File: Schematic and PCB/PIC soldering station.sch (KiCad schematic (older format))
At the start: 69 parts, among them J1 DC_INLET, K2 hakko 907, P1 24VAC, Q1 2N3904, Q2 2N3906, Q3 IRLR2908, SW2 BUTTON1, SW3 BUTTON2, U1 LM358, U2 LM7812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

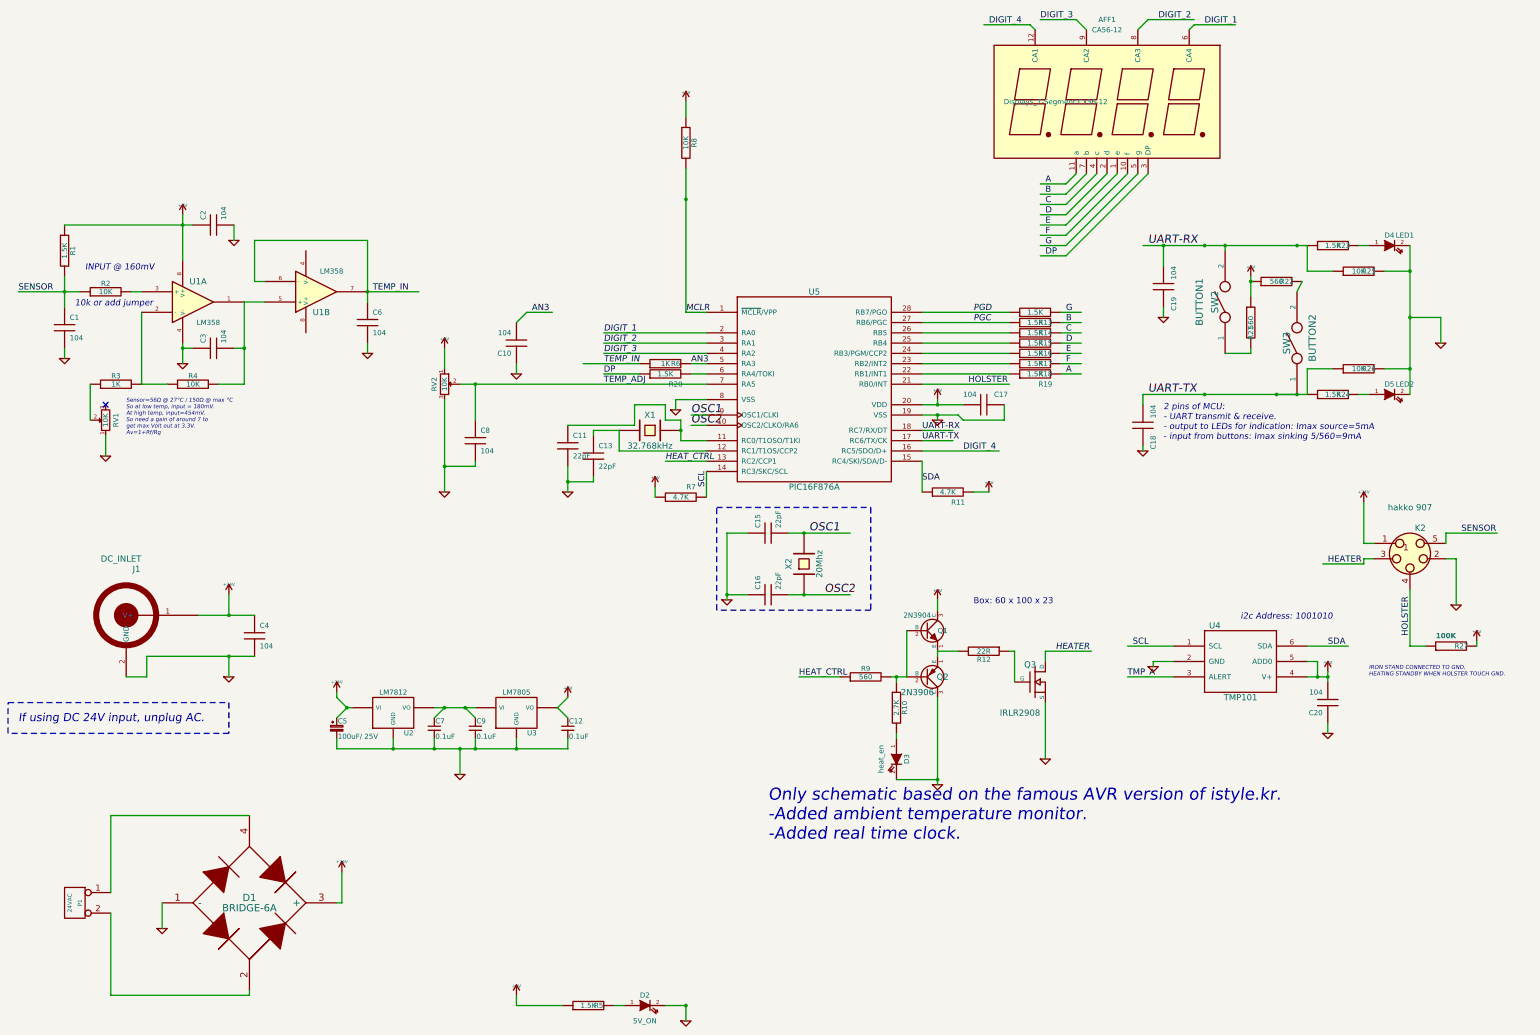
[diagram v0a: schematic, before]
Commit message: Added auto-standby and auto-poweroff; calibration mode
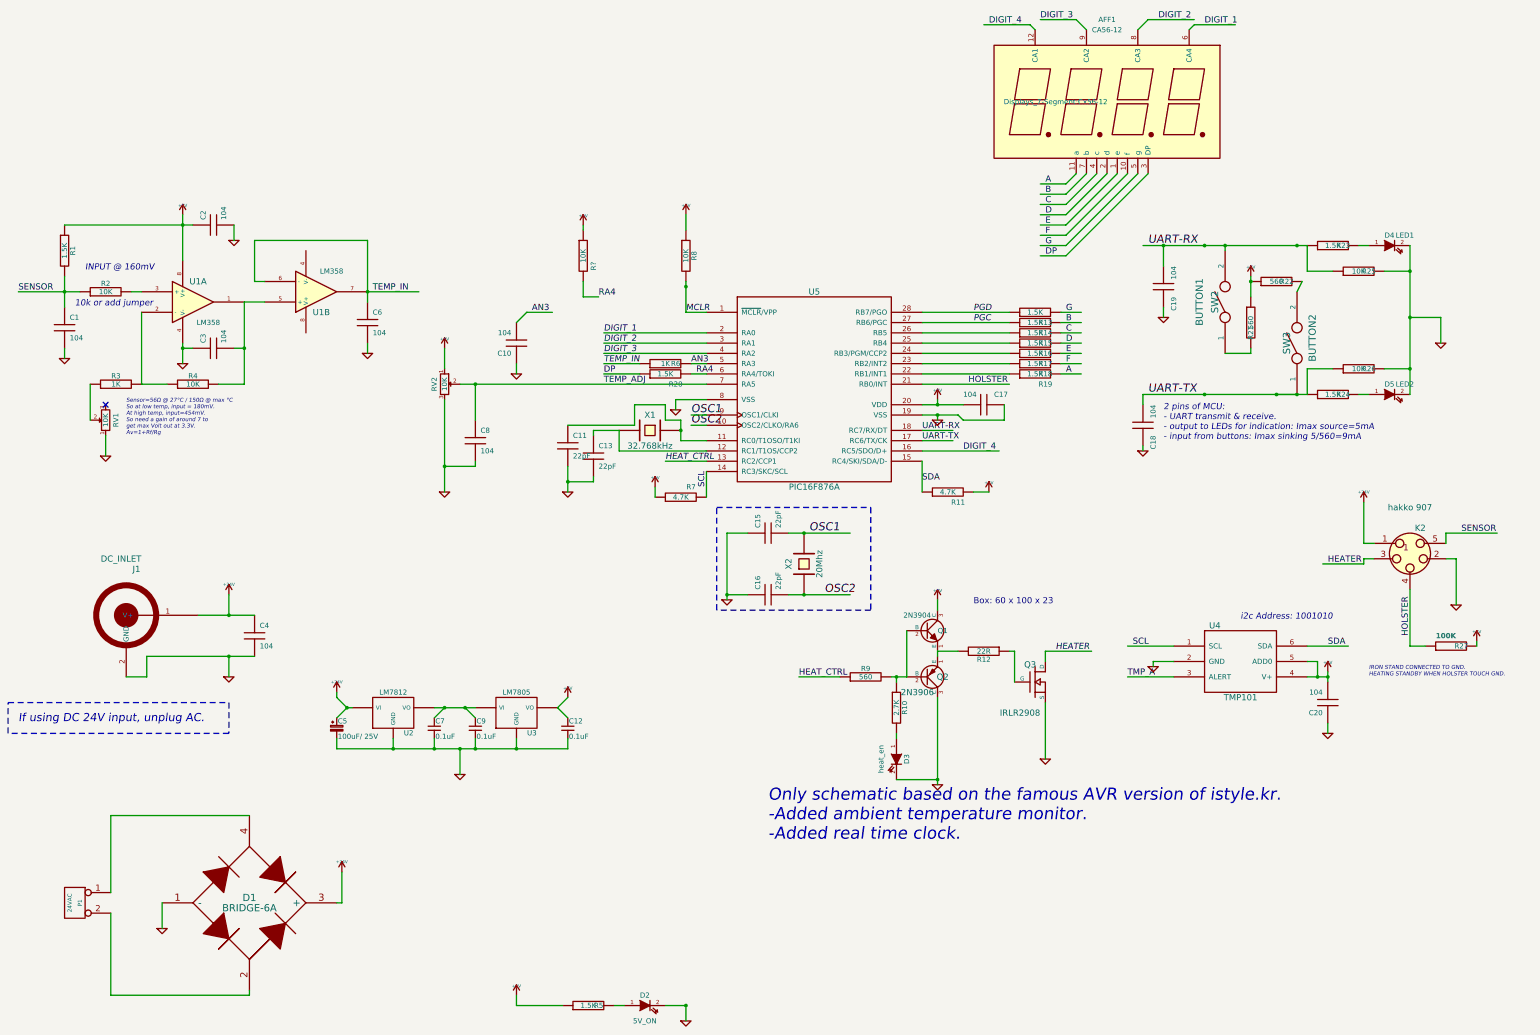
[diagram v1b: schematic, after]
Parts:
- added R?: 10K, Discret:R3, symbol R-RESCUE-PIC_soldering_station
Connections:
- net labels added: RA4
- wire segments 215 -> 259
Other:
- moved on the sheet: R8
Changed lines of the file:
@@
 L R-RESCUE-PIC_soldering_station R8
 U 1 1 564F4FA9
-P 7800 1850
-F 0 "R8" V 7880 1850 50  0000 C CNN
-F 1 "10K" V 7800 1850 50  0000 C CNN
-F 2 "Discret:R3" H 7800 1850 60  0001 C CNN
-F 3 "" H 7800 1850 60  0000 C CNN
-	1    7800 1850
+P 7800 2950
+F 0 "R8" V 7880 2950 50  0000 C CNN
+F 1 "10K" V 7800 2950 50  0000 C CNN
+F 2 "Discret:R3" H 7800 2950 60  0001 C CNN
+F 3 "" H 7800 2950 60  0000 C CNN
+	1    7800 2950
 	1    0    0    -1
 $EndComp
@@
 L +5V #PWR01
 U 1 1 564F6417
-P 7800 1450
-F 0 "#PWR01" H 7800 1540 20  0001 C CNN
-F 1 "+5V" H 7800 1540 30  0000 C CNN
-F 2 "" H 7800 1450 60  0000 C CNN
-F 3 "" H 7800 1450 60  0000 C CNN
-	1    7800 1450
+P 7800 2550
+F 0 "#PWR01" H 7800 2640 20  0001 C CNN
+F 1 "+5V" H 7800 2640 30  0000 C CNN
+F 2 "" H 7800 2550 60  0000 C CNN
+F 3 "" H 7800 2550 60  0000 C CNN
+	1    7800 2550
 	1    0    0    -1
 $EndComp
@@
 	8000 4000 7850 4000
 Wire Wire Line
-	7800 1450 7800 1600
-Wire Wire Line
-	7800 2100 7800 3500
+	7800 2550 7800 2700
+Wire Wire Line
+	7800 3200 7800 3250
+Wire Wire Line
+	7800 3250 7800 3500
 Wire Wire Line
 	7800 3500 8000 3500
 Wire Wire Line
-	10100 4400 10500 4400
+	10100 4400 10250 4400
+Wire Wire Line
+	10250 4400 10500 4400
 Wire Wire Line
 	10250 4400 10250 4350
 Wire Wire Line
-	10100 4500 10450 4500
+	10100 4500 10250 4500
+Wire Wire Line
+	10250 4500 10450 4500
 Wire Wire Line
 	10250 4500 10250 4550
@@
 	15200 5650 15700 5650
 Wire Wire Line
-	1750 3150 1750 3450
-Wire Wire Line
-	1300 3300 1900 3300
+	1750 3150 1750 3300
+Wire Wire Line
+	1750 3300 1750 3450
+Wire Wire Line
+	1300 3300 1750 3300
+Wire Wire Line
+	1750 3300 1900 3300
 Connection ~ 1750 3300
 Wire Wire Line
-	1750 2650 3000 2650
-Wire Wire Line
-	2900 2550 2900 3000
+	1750 2650 2900 2650
+Wire Wire Line
+	2900 2650 3000 2650
+Wire Wire Line
+	2900 2550 2900 2650
+Wire Wire Line
+	2900 2650 2900 3000
 Connection ~ 2900 2650
 Wire Wire Line
@@
 	1750 3850 1750 3950
 Wire Wire Line
-	2900 3800 2900 4000
+	2900 3800 2900 3850
+Wire Wire Line
+	2900 3850 2900 4000
 Wire Wire Line
 	3000 3850 2900 3850
@@
 	2150 4700 2150 4900
 Wire Wire Line
-	3500 3400 3500 4200
+	3500 3400 3500 3850
+Wire Wire Line
+	3500 3850 3500 4200
 Wire Wire Line
 	3500 3850 3400 3850
@@
 	12350 6900 12350 6950
 Wire Wire Line
-	13850 7050 14050 7050
-Wire Wire Line
-	14050 7000 14050 7100
+	13850 7050 13950 7050
+Wire Wire Line
+	13950 7050 14050 7050
+Wire Wire Line
+	14050 7000 14050 7050
+Wire Wire Line
+	14050 7050 14050 7100
 Wire Wire Line
 	13850 6900 13950 6900
@@
 	10100 4750 10400 4750
 Wire Wire Line
-	5600 4200 8000 4200
+	5600 4200 5750 4200
+Wire Wire Line
+	5750 4200 8000 4200
 Wire Wire Line
 	10600 5250 10750 5250
 Wire Wire Line
-	6800 4000 7350 4000
+	7000 4000 7350 4000
 Wire Wire Line
 	11300 7300 11300 7850
@@
 	3400 2650 3400 2800
 Wire Wire Line
-	2550 6850 3600 6850
+	2550 6850 3350 6850
+Wire Wire Line
+	3350 6850 3600 6850
 Wire Wire Line
 	3350 7050 3350 6850
 Connection ~ 3350 6850
 Wire Wire Line
-	3050 6450 3600 6450
+	3050 6450 3350 6450
+Wire Wire Line
+	3350 6450 3600 6450
 Wire Wire Line
 	3350 6250 3350 6450
@@
 	6150 10150 6150 10250
 Wire Wire Line
-	7750 4550 7750 4750
+	7750 4550 7750 4650
+Wire Wire Line
+	7750 4650 7750 4750
 Wire Wire Line
 	7750 4750 8000 4750
@@
 	6900 4650 7150 4650
 Wire Wire Line
-	6650 5000 6650 5250
+	6650 5000 6650 5150
+Wire Wire Line
+	6650 5150 6650 5250
 Wire Wire Line
 	6900 5150 6900 5100
@@
 	8000 4600 7850 4600
 Wire Wire Line
-	8800 5650 9400 5650
-Wire Wire Line
-	8800 6250 9400 6250
+	8800 5650 8950 5650
+Wire Wire Line
+	8950 5650 9400 5650
+Wire Wire Line
+	8800 6250 8950 6250
+Wire Wire Line
+	8950 6250 9400 6250
 Wire Wire Line
 	8400 5650 8200 5650
 Wire Wire Line
-	8200 5650 8200 6300
+	8200 5650 8200 6250
+Wire Wire Line
+	8200 6250 8200 6300
 Wire Wire Line
 	8400 6250 8200 6250
@@
 Connection ~ 8950 5650
 Connection ~ 8950 6250
-Connection ~ 7800 2400
-Wire Wire Line
-	12250 2850 13850 2850
+Connection ~ 7800 3250
+Wire Wire Line
+	12250 2850 12450 2850
+Wire Wire Line
+	12450 2850 12850 2850
+Wire Wire Line
+	12850 2850 13050 2850
+Wire Wire Line
+	13050 2850 13750 2850
+Wire Wire Line
+	13750 2850 13850 2850
 Connection ~ 12850 2850
 Wire Wire Line
-	12250 4300 13850 4300
+	12250 4300 12850 4300
+Wire Wire Line
+	12850 4300 13550 4300
+Wire Wire Line
+	13550 4300 13750 4300
+Wire Wire Line
+	13750 4300 13850 4300
 Connection ~ 12850 4300
 Wire Notes Line
@@
 	5450 3850 5450 4050
 Wire Wire Line
-	5450 4350 5450 5250
+	5450 4350 5450 5000
+Wire Wire Line
+	5450 5000 5450 5250
 Wire Wire Line
 	3500 4200 3250 4200
@@
 	14600 3100 14850 3100
 Wire Wire Line
-	14850 2850 14850 4300
+	14850 2850 14850 3100
+Wire Wire Line
+	14850 3100 14850 3550
+Wire Wire Line
+	14850 3550 14850 4050
+Wire Wire Line
+	14850 4050 14850 4300
 Connection ~ 13750 4300
 Wire Wire Line
@@
 	9950 7050 9950 6600
 Wire Wire Line
-	9800 7050 9950 7050
+	9800 7050 9850 7050
+Wire Wire Line
+	9850 7050 9950 7050
 Wire Wire Line
 	10450 6800 10250 6800
@@
 $EndComp
 Wire Wire Line
-	13300 3150 13300 3350
+	13300 3150 13300 3200
+Wire Wire Line
+	13300 3200 13300 3350
 Wire Wire Line
 	13300 3850 13300 3900
@@
 	9850 8050 10250 8050
 Wire Wire Line
-	10250 7250 10250 8100
+	10250 7250 10250 8050
+Wire Wire Line
+	10250 8050 10250 8100
 Connection ~ 10250 8050
 $Comp
@@
 Connection ~ 4500 7350
 Wire Wire Line
-	5350 7350 5750 7350
+	5350 7350 5450 7350
+Wire Wire Line
+	5450 7350 5650 7350
+Wire Wire Line
+	5650 7350 5750 7350
 Wire Wire Line
 	6550 7350 6650 7450
@@
 	4400 7650 4400 7750
 Wire Wire Line
-	4400 7750 6650 7750
+	4400 7750 4950 7750
+Wire Wire Line
+	4950 7750 5350 7750
+Wire Wire Line
+	5350 7750 5600 7750
+Wire Wire Line
+	5600 7750 5750 7750
+Wire Wire Line
+	5750 7750 6150 7750
+Wire Wire Line
+	6150 7750 6650 7750
 Wire Wire Line
 	6650 7750 6650 7650
@@
 	3600 2800 4700 2800
 Wire Wire Line
-	4700 2800 4700 3400
+	4700 2800 4700 3300
+Wire Wire Line
+	4700 3300 4700 3400
 Text Label 4750 3300 0    60   ~ 0
 TEMP_IN
@@
 AN3
 NoConn ~ 2150 4400
+Text Label 7900 4100 0    60   ~ 0
+RA4
+$Comp
+L R-RESCUE-PIC_soldering_station R?
+U 1 1 571E4B7A
+P 6800 2950
+F 0 "R?" V 6900 2850 50  0000 C CNN
+F 1 "10K" V 6800 2950 50  0000 C CNN
+F 2 "Discret:R3" H 6800 2950 60  0001 C CNN
+F 3 "" H 6800 2950 60  0000 C CNN
+	1    6800 2950
+	1    0    0    -1
+$EndComp
+$Comp
+L +5V #PWR?
+U 1 1 571E5422
+P 6800 2650
+F 0 "#PWR?" H 6800 2740 20  0001 C CNN
+F 1 "+5V" H 6800 2740 30  0000 C CNN
+F 2 "" H 6800 2650 60  0000 C CNN
+F 3 "" H 6800 2650 60  0000 C CNN
+	1    6800 2650
+	1    0    0    -1
+$EndComp
+Wire Wire Line
+	6800 2700 6800 2650
+Wire Wire Line
+	6800 3200 6800 3350
+Wire Wire Line
+	6800 3350 6950 3350
+Text Label 6950 3350 0    60   ~ 0
+RA4
 $EndSCHEMATC
